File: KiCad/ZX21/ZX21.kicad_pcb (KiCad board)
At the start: 2 copper layers, 142 x 100 mm, 128 parts, among them IC1 ULA 2C210E, IC101 555, IC102 74HCT00, IC2 AT28C256, IC3 Z80A, IC301 3V3 PSU, IC302 ESP32-WROOM, IC303 AZ1117-3.3, IC4 62256, IC501 YM2149, IC502 GAL16V8, IC801 AS6C4008Extra, J1 Jack-DC, J2 Conn_01x02, J203 Conn_01x03, J204 Conn_01x03, J301 Conn_01x04, J401 DB9_Male, J501 Conn_01x06, J502 Conn_01x08, J503 Conn_01x08, J504 Conn_01x07, J601 Conn_02x08_Odd_Even, J701 Conn_02x23_Row_Letter_First, J702 Conn_01x09, J703 Conn_01x09, X1 3.5MHz, X501 ECS-100AX-040

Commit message: Yup more routing
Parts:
- removed J2: Conn_01x02, Pin_Headers:Pin_Header_Straight_1x02_Pitch2.54mm
- removed X501: ECS-100AX-040, Oscillators:Oscillator_DIP-14
- added J101: Conn_01x03, Pin_Headers:Pin_Header_Straight_1x03_Pitch2.54mm, F.Cu at (140.3, 95.2)
- added R106: 10K, Resistors_SMD:R_0603_HandSoldering, B.Cu at (137.8, 91.9)
- R105: value 4K7 -> 10K
- moved R30 33.1 mm to (90.8, 54.6), turned to 270 degrees
- moved R6 26.9 mm to (87.3, 81.3), turned to 90 degrees
- moved R2 21.1 mm to (106.7, 49.2)
- moved C2 20.8 mm to (66.0, 39.4)
- moved R105 12.2 mm to (135.3, 91.9), turned to 90 degrees
- moved C5 6.59 mm to (98.1, 45.4), turned to 90 degrees
- moved R15 5.54 mm to (109.5, 46.0), turned to 180 degrees
- moved R33 3.18 mm to (66.4, 90.2)
- moved TR2 3.17 mm to (90.5, 69.2)
- moved C105 3.14 mm to (123.2, 84.5)
- moved J504 3.00 mm to (107.0, 120.7)
- moved X1 2.56 mm to (90.8, 47.6)
- moved R17 2.48 mm to (86.7, 43.8)
- moved IC102 2.22 mm to (121.6, 79.1)
- moved R1 1.59 mm to (90.2, 81.3)
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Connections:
- IC102 pad 13: Net-(IC102-Pad1) -> Net-(IC102-Pad13)
- J504 pad 2: Net-(J504-Pad2) -> Net-(IC501-Pad28)
- J504 pad 3: Net-(IC501-Pad28) -> Net-(IC501-Pad25)
- J504 pad 4: Net-(IC501-Pad25) -> Net-(IC501-Pad24)
- J504 pad 5: Net-(IC501-Pad24) -> Net-(IC501-Pad23)
- J504 pad 6: Net-(IC501-Pad23) -> Net-(IC501-Pad22)
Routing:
- net GND: track 508.3 -> 748.6 mm, vias 3 -> 9
- net +5V: track 356.8 -> 526.5 mm, vias 0 -> 5
- net IORQ: track 9.53 -> 176.7 mm, vias 0 -> 4
- net WR: track 97.4 -> 227.6 mm, vias 2 -> 8
- net WAIT: track 9.62 -> 110.8 mm, vias 0 -> 2
- net NMI: track 104.6 -> 185.5 mm, vias 4 -> 6
- net Net-(IC501-Pad22): track 71.4 -> 4.13 mm, vias 2 -> 0
- net D7': track 121.9 -> 186.4 mm, vias 1 -> 3
- net HALT: track 101.2 -> 164.3 mm, vias 1 -> 3
- net D0': track 119.2 -> 179.3 mm, vias 0 -> 1
- net D5': track 113.7 -> 170.9 mm, vias 1 -> 2
- net MI: track 122.1 -> 177.9 mm
- net A15: track 149.8 -> 205.4 mm, vias 3 -> 5
- net D4': track 126.0 -> 181.0 mm, vias 1 -> 2
- net D3': track 117.5 -> 171.7 mm, vias 1 -> 2
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
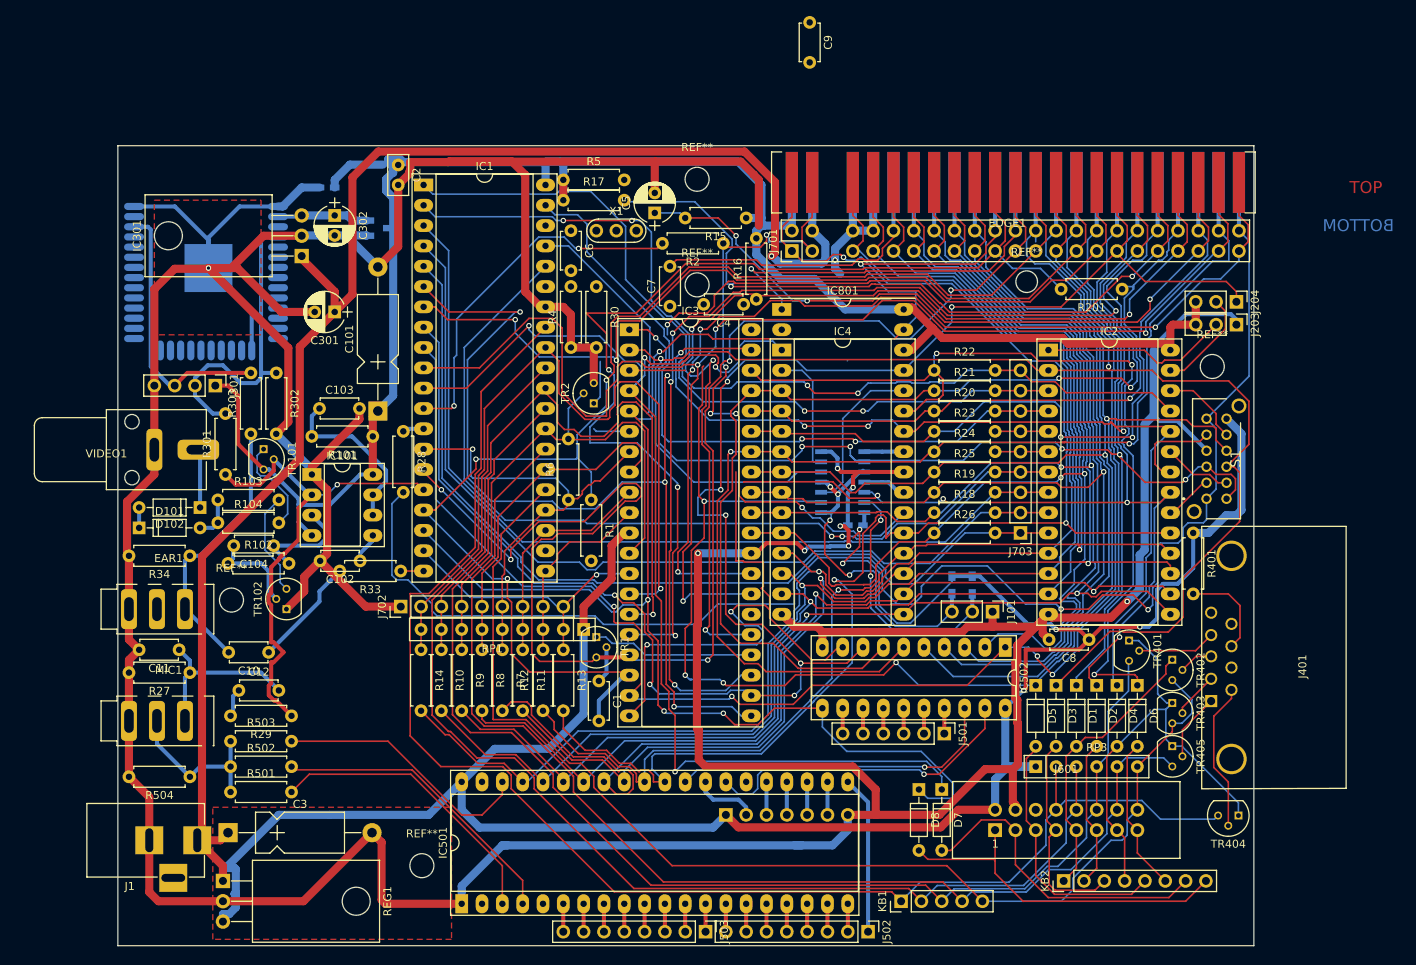
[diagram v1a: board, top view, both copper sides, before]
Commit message: Added option for YMZ284 :D
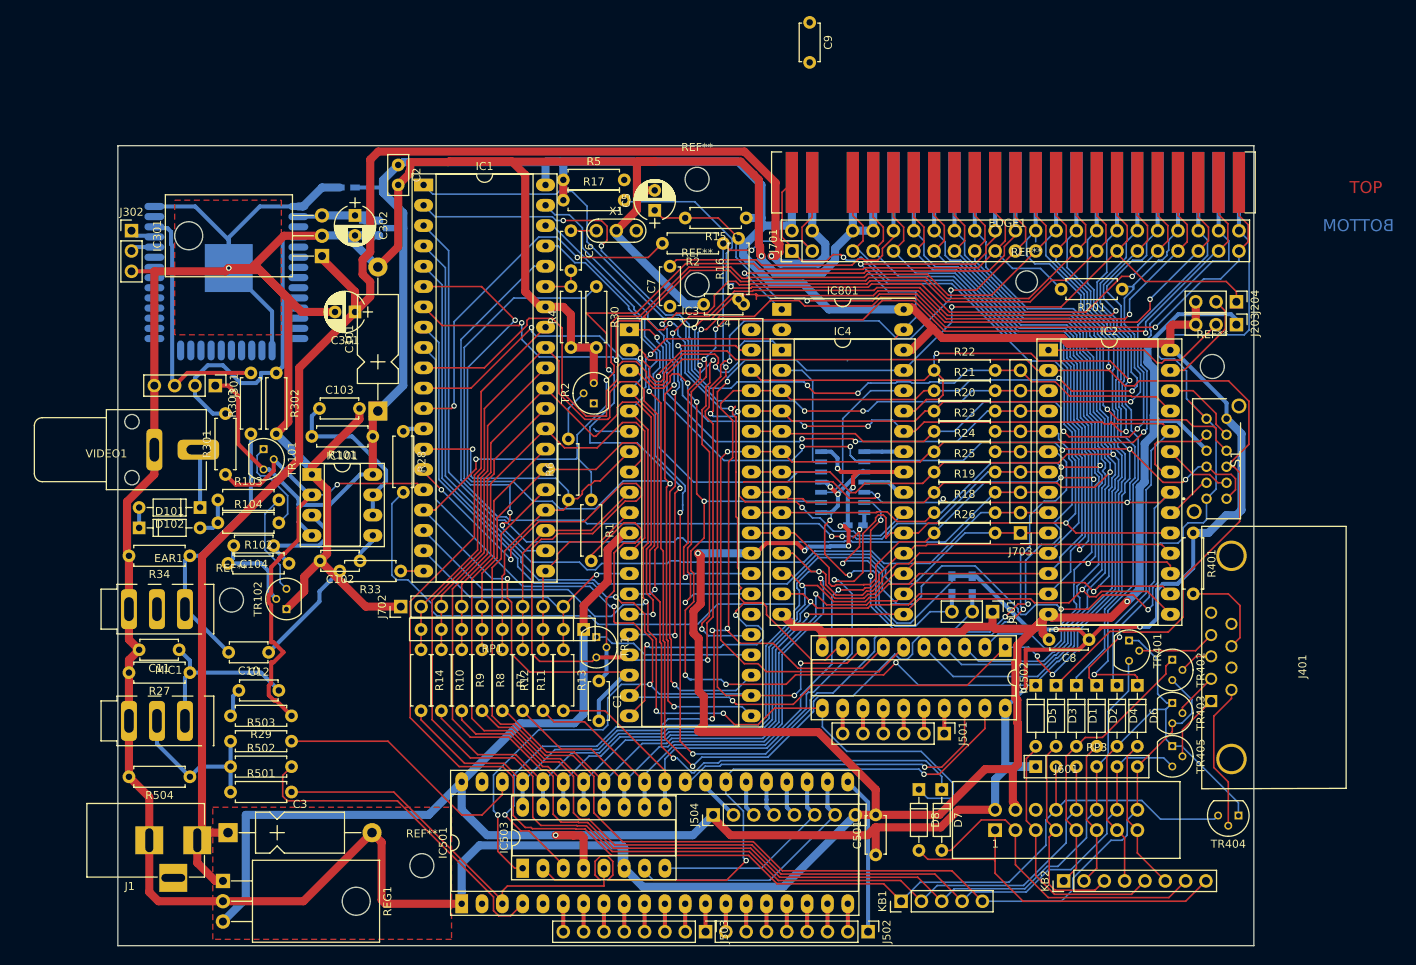
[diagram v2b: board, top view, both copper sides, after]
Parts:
- added C501: 100N, Capacitors_THT:C_Disc_D4.7mm_W2.5mm_P5.00mm, F.Cu at (125.7, 125.7)
- added IC503: YMZ284, Housings_DIP:DIP-16_W7.62mm_Socket_LongPads, F.Cu at (81.6, 127.3)
- added J302: Conn_01x03, Pin_Headers:Pin_Header_Straight_1x03_Pitch2.54mm, F.Cu at (32.7, 47.6)
- J504: value Conn_01x07 -> Conn_01x08; footprint Pin_Headers:Pin_Header_Straight_1x07_Pitch2.54mm -> Pin_Headers:Pin_Header_Straight_1x08_Pitch2.54mm; moved to F.Cu
- moved C301 2.54 mm to (60.6, 57.8)
- moved C302 2.54 mm to (60.6, 45.7)
- moved C303 2.54 mm to (59.7, 42.2)
- moved IC301 2.54 mm to (56.5, 50.8)
- moved IC302 2.54 mm to (44.6, 49.8)
- moved R16 2.22 mm to (108.6, 56.2)
- moved J504 1.59 mm to (105.4, 120.7), turned to 90 degrees
- moved C5 0.32 mm to (98.1, 45.1)
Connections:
- J504 pad 3: Net-(IC501-Pad25) -> Net-(IC501-Pad26)
- J504 pad 4: Net-(IC501-Pad24) -> Net-(IC501-Pad25)
- J504 pad 5: Net-(IC501-Pad23) -> Net-(IC501-Pad24)
- J504 pad 6: Net-(IC501-Pad22) -> Net-(IC501-Pad23)
- J504 pad 7: GND -> Net-(IC501-Pad22)
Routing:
- net A5': track 6.67 -> 160.6 mm, vias 0 -> 4
- net A4': track 34.8 -> 157.9 mm, vias 0 -> 4
- net GND: track 748.6 -> 812.7 mm
- net A7: track 135.3 -> 194.4 mm, vias 2 -> 6
- net Net-(IC1-Pad22): track 0.00 -> 54.8 mm, vias 0 -> 2
- net Net-(IC501-Pad27): track 40.4 -> 83.6 mm, vias 1 -> 2
- net WR: track 227.6 -> 263.5 mm, vias 8 -> 7
- net Net-(IC501-Pad22): track 4.13 -> 32.6 mm
- net IORQ: track 176.7 -> 203.4 mm, vias 4 -> 6
- net Net-(C1-Pad1): track 4.60 -> 31.0 mm
- net +5V: track 526.5 -> 548.8 mm, vias 5 -> 6
- net Net-(IC501-Pad23): track 4.13 -> 26.0 mm
- net ROM_CS: track 187.5 -> 203.2 mm
- net Net-(IC501-Pad3): track 36.8 -> 49.1 mm
- net D4': track 181.0 -> 173.6 mm
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
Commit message: Routed!
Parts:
- moved C4 57.7 mm to (87.9, 110.5), turned to 0 degrees
- moved C9 44.1 mm to (135.3, 61.9), turned to 0 degrees
- moved R5 43.7 mm to (91.1, 84.8), turned to 90 degrees
- moved R1 2.56 mm to (87.9, 82.5)
- moved R17 1.93 mm to (87.0, 41.9)
- moved R16 1.35 mm to (109.5, 57.1)
- moved R6 1.14 mm to (87.9, 80.3)
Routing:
- net RESET: track 90.1 -> 146.1 mm, vias 3 -> 5
- net WAIT: track 110.9 -> 162.1 mm, vias 2 -> 4
- net CLK: track 61.8 -> 102.1 mm, vias 1 -> 2
- net GND: track 812.7 -> 847.9 mm, vias 9 -> 10
- net NMI: track 185.6 -> 157.3 mm
- net A10: track 130.4 -> 152.0 mm, vias 4 -> 5
- net Net-(C7-Pad1): track 6.50 -> 25.0 mm
- net Net-(C1-Pad1): track 31.0 -> 17.7 mm
- net IORQ: track 203.4 -> 194.1 mm
- net INT: track 131.9 -> 122.8 mm
- net Net-(IC3-Pad6): track 4.58 -> 12.0 mm
- net +5V: track 548.8 -> 553.5 mm
- net RD: track 194.7 -> 198.7 mm
- net A14: track 201.3 -> 205.2 mm
- net D7: track 35.7 -> 39.3 mm
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
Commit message: Tidy Up
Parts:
- J504: moved to B.Cu
- moved KB1 0.63 mm to (128.3, 131.4)
- turned J504 to 270 degrees
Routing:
- net Net-(IC501-Pad27): track 83.6 -> 74.1 mm
- net GND: track 847.9 -> 842.6 mm
- net Net-(IC501-Pad4): track 42.0 -> 45.7 mm
- net +9V: track 192.2 -> 195.7 mm
- net Net-(IC501-Pad38): track 32.8 -> 29.8 mm
- net Net-(IC501-Pad3): track 49.1 -> 52.0 mm
- net ROM_CS: track 204.0 -> 202.9 mm
- net IORQ: track 194.1 -> 192.9 mm
- net A9: track 152.1 -> 151.3 mm
- net Net-(IC501-Pad23): track 26.0 -> 26.8 mm
- net WR: track 265.1 -> 264.5 mm
- net Net-(IC501-Pad22): track 32.6 -> 33.1 mm
- net KBD0: track 182.8 -> 183.3 mm

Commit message: Into DRC
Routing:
- net GND: track 842.6 -> 827.6 mm
- net D5': track 174.5 -> 175.2 mm
- net D3': track 175.7 -> 176.4 mm
- net D6': track 169.0 -> 169.6 mm
- net D7: track 39.3 -> 38.8 mm
- net NMI: vias 6 -> 5

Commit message: Fixing DRC Issues
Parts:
- C1: footprint Capacitors_THT:C_Disc_D4.7mm_W2.5mm_P5.00mm -> Capacitors_THT:C_Disc_D3.0mm_W2.0mm_P2.50mm
- C10, C102, C103, C104, C11, C12, C4, C501, C6, C7, C8, C9: footprint Capacitors_THT:C_Disc_D4.7mm_W2.5mm_P5.00mm -> Capacitors_ThroughHole:C_Disc_D4.7mm_W2.5mm_P5.00mm
- C3: footprint Capacitors_THT:CP_Axial_L11.0mm_D5.0mm_P18.00mm_Horizontal -> Capacitors_ThroughHole:CP_Axial_L11.0mm_D5.0mm_P18.00mm_Horizontal
- C301, C302, C5: footprint Capacitors_THT:CP_Radial_D5.0mm_P2.50mm -> Capacitors_ThroughHole:CP_Radial_D5.0mm_P2.50mm
- D1, D101, D102, D2, D3, D4, D5, D6, D7, D8: footprint Diodes_THT:D_DO-35_SOD27_P7.62mm_Horizontal -> zxbus:D_DO-35_SOD27_P7.62mm_Horizontal
- R1, R10, R101, R102, R103, R104, R11, R12, R13, R14, R15, R16, R17, R18, R19, R2, R20, R201, R21, R22, R23, R24, R25, R26, R27, R28, R29, R30, R301, R302, R303, R33, R34, R4, R401, R5, R501, R502, R503, R504, R6, R7, R8, R9: footprint Resistors_ThroughHole:R_Axial_DIN0207_L6.3mm_D2.5mm_P7.62mm_Horizontal -> Resistors_ThroughHole:R_Axial_DIN0204_L3.6mm_D1.6mm_P7.62mm_Horizontal
- moved R33 8.04 mm to (58.4, 91.4), turned to 270 degrees
- moved TR1 5.09 mm to (91.1, 103.5), turned to 90 degrees
- moved C301 1.91 mm to (58.7, 57.8)
- moved C1 1.89 mm to (90.8, 105.8)
- moved D8 0.63 mm to (130.5, 117.5)
- moved R28 0.45 mm to (66.4, 72.4)
- moved D7 0.32 mm to (133.7, 117.5)
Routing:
- net Net-(IC1-Pad20): track 2.86 -> 11.3 mm
- net Net-(C10-Pad1): track 13.8 -> 9.10 mm
- net Net-(IC501-Pad21): track 19.8 -> 22.9 mm
- net GND: track 827.6 -> 824.8 mm
- net +9V: track 195.7 -> 197.6 mm
- net HALT: track 163.0 -> 161.2 mm
- net MREQ: track 190.0 -> 188.9 mm
- net A15: track 203.6 -> 204.6 mm
- net Net-(C1-Pad1): track 17.7 -> 16.8 mm

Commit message: Fixing DRC Issues
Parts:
- J502, J503, J504: footprint Pin_Headers:Pin_Header_Straight_1x08_Pitch2.54mm -> zxbus:Pin_Header_Straight_1x08_Pitch2.54mm
- moved R101 6.70 mm to (59.4, 67.6), turned to 270 degrees
- moved C104 5.62 mm to (54.3, 91.1)
- moved C103 5.33 mm to (56.5, 75.2), turned to 90 degrees
- moved TR101 2.84 mm to (47.9, 77.5), turned to 0 degrees
- moved X1 2.01 mm to (92.7, 47.0), turned to 270 degrees
- moved C7 1.98 mm to (98.1, 56.5)
- moved TR102 1.93 mm to (51.8, 96.8)
- moved C1 1.77 mm to (89.5, 107.0), turned to 0 degrees
- moved C5 1.71 mm to (97.5, 46.7)
- moved C102 1.62 mm to (62.9, 89.2)
- moved R102 1.59 mm to (43.5, 88.3)
- moved R33 1.31 mm to (58.1, 92.7)
- moved R17 1.27 mm to (87.0, 40.6)
- moved TR402 1.25 mm to (162.8, 100.0)
- moved C4 1.00 mm to (87.6, 111.4)
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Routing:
- net GND: track 824.8 -> 812.2 mm
- net +5V: track 553.5 -> 561.0 mm
- net Net-(C103-Pad1): track 21.2 -> 15.9 mm
- net Net-(R103-Pad2): track 12.9 -> 17.3 mm
- net Net-(C102-Pad1): track 3.83 -> 0.00 mm
- net Net-(R104-Pad2): track 12.1 -> 9.40 mm
- net +9V: track 197.6 -> 199.8 mm
- net KBD4: track 151.7 -> 153.9 mm
- net IORQ: track 192.9 -> 195.1 mm
- net Net-(C6-Pad1): track 3.18 -> 5.21 mm
- net D7': track 186.6 -> 188.6 mm
- net Net-(C104-Pad1): track 13.5 -> 15.5 mm
- net A8': track 113.7 -> 115.6 mm
- net A5': track 160.3 -> 162.1 mm
- net A6': track 83.3 -> 85.1 mm
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
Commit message: FIrst go at DRC complete
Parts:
- removed the REF** at (144.6, 54.0)
- added REF**: MountingHole_2.7mm, zxbus:MountingHole_2.7mm, F.Cu at (144.6, 54.0)
- C303, IC302, IC303: moved to F.Cu
- J101, J203, J204, J302: footprint Pin_Headers:Pin_Header_Straight_1x03_Pitch2.54mm -> zxbus:Pin_Header_Straight_1x03_Pitch2.54mm
- S1: footprint SamacSys_Parts:EG4208A -> SamacSys_Parts:EG4208
- moved C101 41.4 mm to (22.9, 66.7)
- moved J302 21.9 mm to (54.6, 48.3)
- moved R504 18.6 mm to (58.4, 118.7), turned to 0 degrees
- moved C11 16.5 mm to (45.1, 115.3), turned to 0 degrees
- moved R501 13.4 mm to (58.4, 116.2)
- moved R502 13.4 mm to (58.4, 113.7)
- moved R503 13.3 mm to (58.4, 111.1)
- moved R27 12.4 mm to (40.3, 115.3)
- moved IC301 8.45 mm to (63.5, 55.6)
- moved C12 7.76 mm to (50.1, 111.8), turned to 180 degrees
- moved IC303 7.23 mm to (56.5, 45.8), turned to 270 degrees
- moved R28 6.04 mm to (66.0, 78.4)
- moved C302 5.02 mm to (59.1, 50.5)
- moved X1 4.77 mm to (87.9, 46.7), turned to 90 degrees
- moved R17 4.13 mm to (91.1, 40.6)
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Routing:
- net GND: track 812.2 -> 775.2 mm, vias 10 -> 9
- net +3V3: track 11.4 -> 47.1 mm
- net Net-(IC501-Pad4): track 45.7 -> 24.5 mm
- net SOUND: track 20.6 -> 37.8 mm
- net Net-(IC501-Pad3): track 52.0 -> 37.2 mm
- net Net-(IC501-Pad38): track 29.8 -> 18.3 mm
- net VP: track 38.8 -> 48.4 mm
- net ROM_CS: track 203.1 -> 195.3 mm
- net Net-(C11-Pad1): track 21.7 -> 15.1 mm
- net Net-(IC1-Pad13): track 2.86 -> 7.72 mm
- net +9V: track 199.8 -> 195.2 mm
- net Net-(C12-Pad1): track 3.60 -> 7.48 mm
- net Net-(C102-Pad1): track 0.00 -> 3.49 mm
- net WAIT: track 162.9 -> 159.5 mm
- net A8: track 136.9 -> 134.1 mm
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- added copper zone on B.Cu, net GND
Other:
- rule trace_min: 0.2 -> 0
